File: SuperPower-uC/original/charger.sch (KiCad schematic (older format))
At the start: 34 parts, among them J1 Conn_01x02_Male, J2 Conn_01x02_Male, Q1 Q_NMOS_DGS, Q2 Q_NMOS_DGS, Q3 Q_NMOS_DGS, Q4 Q_PMOS_DGS, U1 LTC4162-L

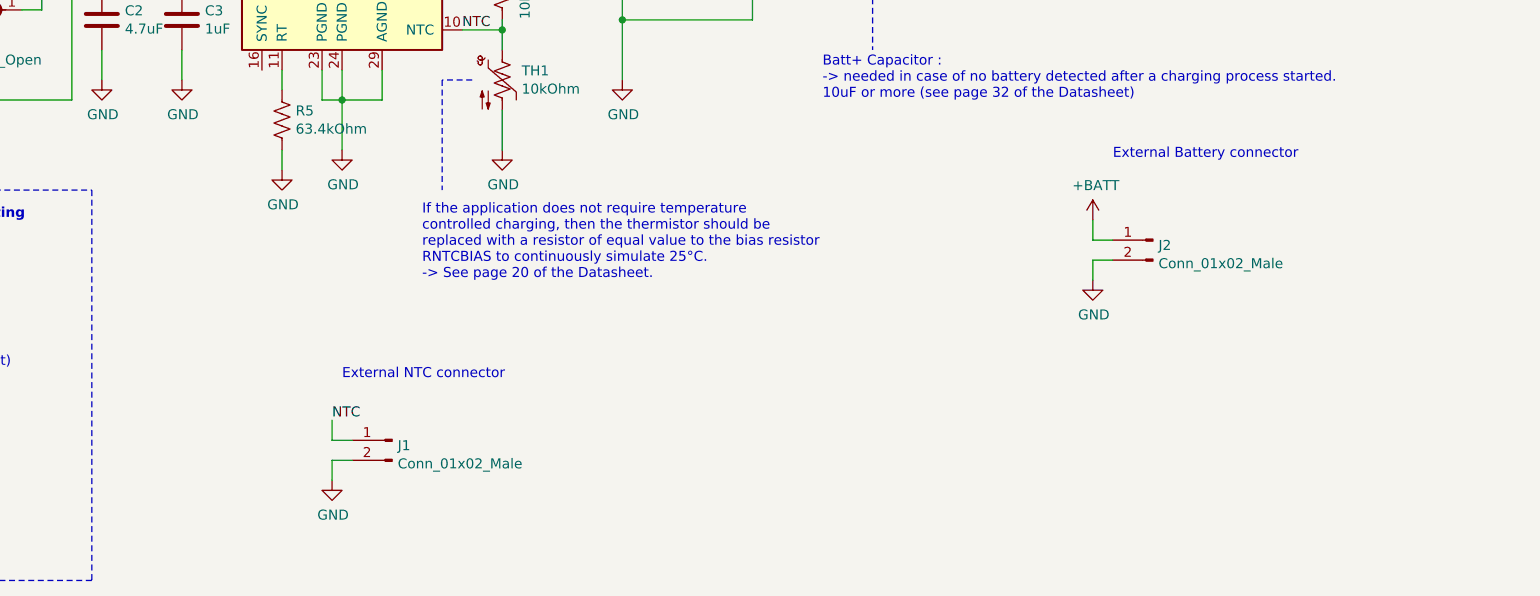
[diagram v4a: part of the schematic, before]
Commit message: Add default 1 cell settings
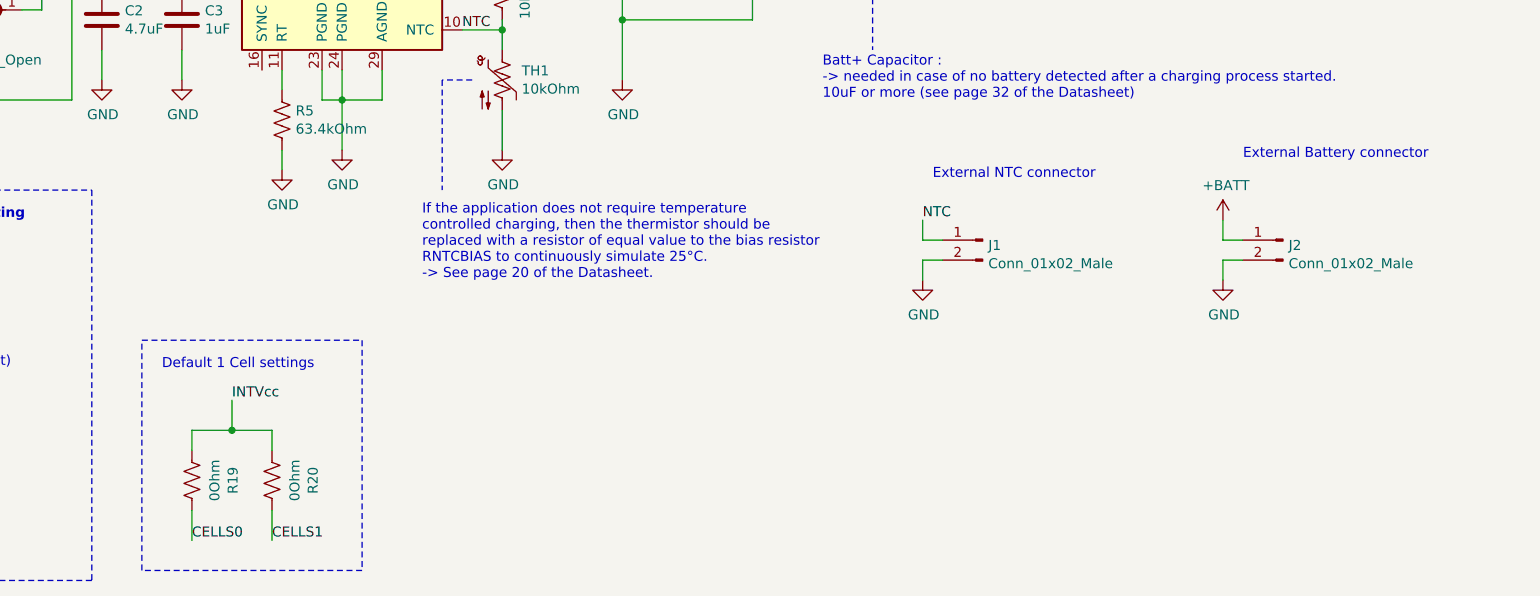
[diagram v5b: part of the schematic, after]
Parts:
- added R19, R20: 0Ohm, symbol Device:R_US
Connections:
- net CELLS0: now also R19.1
- net CELLS1: now also R20.1
- net INTVcc: now also R19.2, R20.2
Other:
- note added: "Default 1 Cell settings"
- moved on the sheet: J1, J2
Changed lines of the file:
@@
 L Connector:Conn_01x02_Male J1
 U 1 1 5F8314D1
-P 5850 6950
-F 0 "J1" H 5822 6924 50  0000 R CNN
-F 1 "Conn_01x02_Male" H 5822 6833 50  0000 R CNN
-F 2 "" H 5850 6950 50  0001 C CNN
-F 3 "~" H 5850 6950 50  0001 C CNN
-	1    5850 6950
+P 8800 5950
+F 0 "J1" H 8772 5924 50  0000 R CNN
+F 1 "Conn_01x02_Male" H 8772 5833 50  0000 R CNN
+F 2 "" H 8800 5950 50  0001 C CNN
+F 3 "~" H 8800 5950 50  0001 C CNN
+	1    8800 5950
 	-1   0    0    -1
 $EndComp
@@
 L power:GND #PWR07
 U 1 1 5F832657
-P 5550 7150
-F 0 "#PWR07" H 5550 6900 50  0001 C CNN
-F 1 "GND" H 5555 6977 50  0000 C CNN
-F 2 "" H 5550 7150 50  0001 C CNN
-F 3 "" H 5550 7150 50  0001 C CNN
-	1    5550 7150
-	1    0    0    -1
-$EndComp
-Wire Wire Line
-	5550 7150 5550 7050
-Wire Wire Line
-	5550 7050 5650 7050
-Wire Wire Line
-	5650 6950 5550 6950
-Wire Wire Line
-	5550 6950 5550 6850
-Text Label 5550 6850 0    50   ~ 0
+P 8500 6150
+F 0 "#PWR07" H 8500 5900 50  0001 C CNN
+F 1 "GND" H 8505 5977 50  0000 C CNN
+F 2 "" H 8500 6150 50  0001 C CNN
+F 3 "" H 8500 6150 50  0001 C CNN
+	1    8500 6150
+	1    0    0    -1
+$EndComp
+Wire Wire Line
+	8500 6150 8500 6050
+Wire Wire Line
+	8500 6050 8600 6050
+Wire Wire Line
+	8600 5950 8500 5950
+Wire Wire Line
+	8500 5950 8500 5850
+Text Label 8500 5850 0    50   ~ 0
 NTC
 Connection ~ 3150 2700
@@
 Wire Wire Line
 	2500 2700 3150 2700
-Text Notes 5600 6650 0    50   ~ 0
+Text Notes 8550 5650 0    50   ~ 0
 External NTC connector
 Wire Notes Line
@@
 L Connector:Conn_01x02_Male J2
 U 1 1 5F831EE9
-P 9650 5950
-F 0 "J2" H 9622 5924 50  0000 R CNN
-F 1 "Conn_01x02_Male" H 9622 5833 50  0000 R CNN
-F 2 "" H 9650 5950 50  0001 C CNN
-F 3 "~" H 9650 5950 50  0001 C CNN
-	1    9650 5950
+P 10300 5950
+F 0 "J2" H 10272 5924 50  0000 R CNN
+F 1 "Conn_01x02_Male" H 10272 5833 50  0000 R CNN
+F 2 "" H 10300 5950 50  0001 C CNN
+F 3 "~" H 10300 5950 50  0001 C CNN
+	1    10300 5950
 	-1   0    0    -1
 $EndComp
@@
 L power:GND #PWR016
 U 1 1 5F831EF3
-P 9350 6150
-F 0 "#PWR016" H 9350 5900 50  0001 C CNN
-F 1 "GND" H 9355 5977 50  0000 C CNN
-F 2 "" H 9350 6150 50  0001 C CNN
-F 3 "" H 9350 6150 50  0001 C CNN
-	1    9350 6150
-	1    0    0    -1
-$EndComp
-Wire Wire Line
-	9350 6150 9350 6050
-Wire Wire Line
-	9350 6050 9450 6050
-Wire Wire Line
-	9450 5950 9350 5950
-Wire Wire Line
-	9350 5950 9350 5850
+P 10000 6150
+F 0 "#PWR016" H 10000 5900 50  0001 C CNN
+F 1 "GND" H 10005 5977 50  0000 C CNN
+F 2 "" H 10000 6150 50  0001 C CNN
+F 3 "" H 10000 6150 50  0001 C CNN
+	1    10000 6150
+	1    0    0    -1
+$EndComp
+Wire Wire Line
+	10000 6150 10000 6050
+Wire Wire Line
+	10000 6050 10100 6050
+Wire Wire Line
+	10100 5950 10000 5950
+Wire Wire Line
+	10000 5950 10000 5850
 $Comp
 L power:+BATT #PWR015
 U 1 1 5F837E39
-P 9350 5850
-F 0 "#PWR015" H 9350 5700 50  0001 C CNN
-F 1 "+BATT" H 9365 6023 50  0000 C CNN
-F 2 "" H 9350 5850 50  0001 C CNN
-F 3 "" H 9350 5850 50  0001 C CNN
-	1    9350 5850
-	1    0    0    -1
-$EndComp
-Text Notes 9450 5550 0    50   ~ 0
+P 10000 5850
+F 0 "#PWR015" H 10000 5700 50  0001 C CNN
+F 1 "+BATT" H 10015 6023 50  0000 C CNN
+F 2 "" H 10000 5850 50  0001 C CNN
+F 3 "" H 10000 5850 50  0001 C CNN
+	1    10000 5850
+	1    0    0    -1
+$EndComp
+Text Notes 10100 5550 0    50   ~ 0
 External Battery connector
 $Comp
@@
 Text Notes 3200 3850 0    50   ~ 0
 TODO : Add Hierarchical Block Connector ->
+$Comp
+L Device:R_US R19
+U 1 1 5F845E81
+P 4850 7150
+F 0 "R19" V 4645 7150 50  0000 C CNN
+F 1 "0Ohm" V 4736 7150 50  0000 C CNN
+F 2 "" V 4890 7140 50  0001 C CNN
+F 3 "~" H 4850 7150 50  0001 C CNN
+	1    4850 7150
+	-1   0    0    1
+$EndComp
+$Comp
+L Device:R_US R20
+U 1 1 5F846819
+P 5250 7150
+F 0 "R20" V 5045 7150 50  0000 C CNN
+F 1 "0Ohm" V 5136 7150 50  0000 C CNN
+F 2 "" V 5290 7140 50  0001 C CNN
+F 3 "~" H 5250 7150 50  0001 C CNN
+	1    5250 7150
+	-1   0    0    1
+$EndComp
+Wire Wire Line
+	4850 7300 4850 7450
+Wire Wire Line
+	5250 7450 5250 7300
+Wire Wire Line
+	4850 7000 4850 6900
+Wire Wire Line
+	5250 7000 5250 6900
+Text Label 4850 7450 0    50   ~ 0
+CELLS0
+Text Label 5250 7450 0    50   ~ 0
+CELLS1
+Text Notes 4700 6600 0    50   ~ 0
+Default 1 Cell settings
+Wire Wire Line
+	4850 6900 5050 6900
+Wire Wire Line
+	5050 6750 5050 6900
+Connection ~ 5050 6900
+Wire Wire Line
+	5050 6900 5250 6900
+Text Label 5050 6750 0    50   ~ 0
+INTVcc
+Wire Notes Line
+	4600 6450 5700 6450
+Wire Notes Line
+	5700 6450 5700 7600
+Wire Notes Line
+	5700 7600 4600 7600
+Wire Notes Line
+	4600 7600 4600 6450
 $EndSCHEMATC

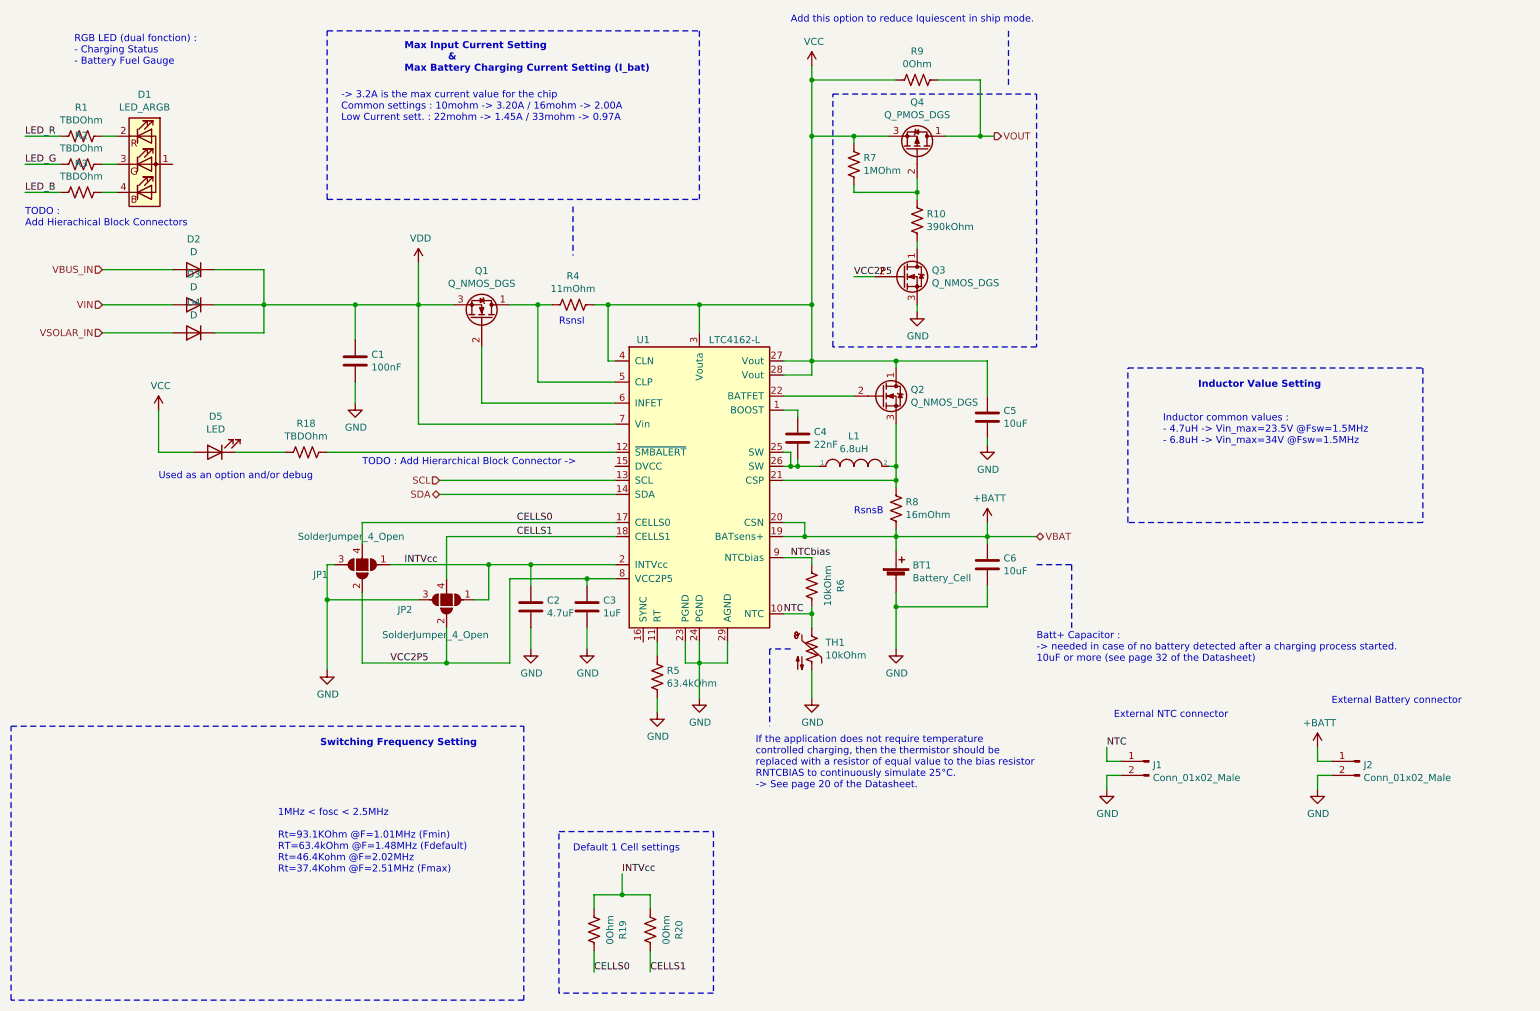
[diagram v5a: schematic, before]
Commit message: Update components annotations
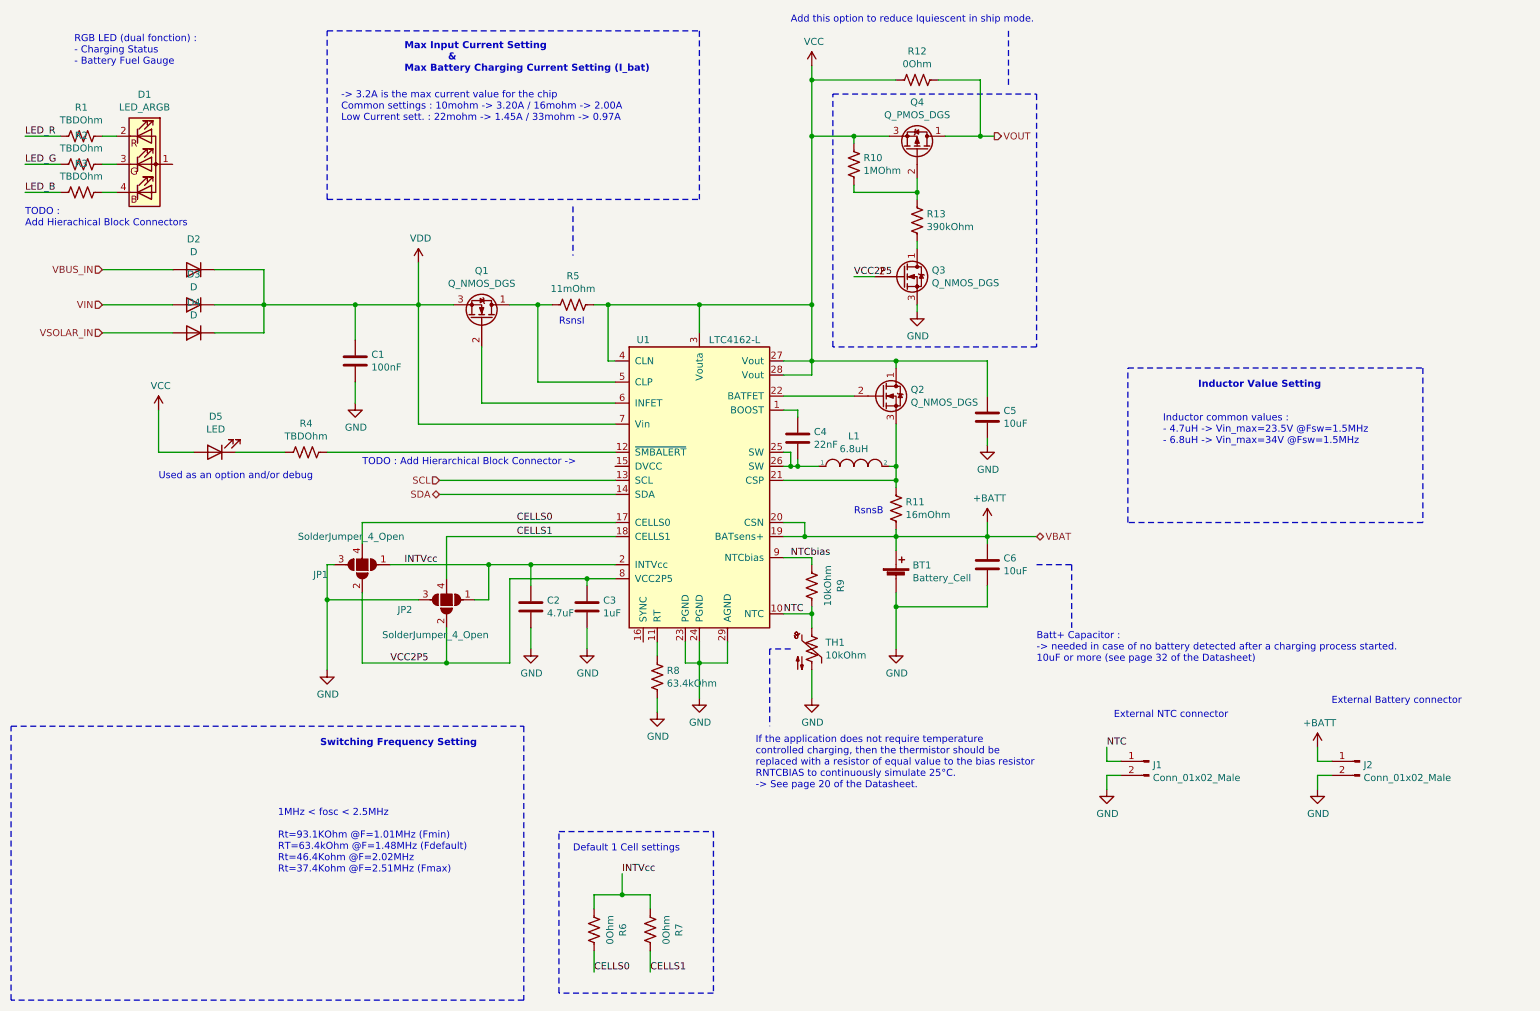
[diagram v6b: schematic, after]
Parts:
- renumbered R7 to R10, R8 to R11, R9 to R12, R10 to R13, R18 to R4, R4 to R5, R19 to R6, R20 to R7, R5 to R8, R6 to R9
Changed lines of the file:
@@
 $EndComp
 $Comp
-L Device:R_US R4
+L Device:R_US R5
 U 1 1 5F743F05
 P 4700 2700
-F 0 "R4" V 4495 2700 50  0000 C CNN
+F 0 "R5" V 4495 2700 50  0000 C CNN
 F 1 "11mOhm" V 4586 2700 50  0000 C CNN
 F 2 "" V 4740 2690 50  0001 C CNN
@@
 $EndComp
 $Comp
-L power:VDD #PWR03
+L power:VDD #PWR04
 U 1 1 5F7457C8
 P 3600 2400
-F 0 "#PWR03" H 3600 2250 50  0001 C CNN
+F 0 "#PWR04" H 3600 2250 50  0001 C CNN
 F 1 "VDD" H 3615 2573 50  0000 C CNN
 F 2 "" H 3600 2400 50  0001 C CNN
@@
 Connection ~ 4950 2700
 $Comp
-L power:GND #PWR02
+L power:GND #PWR03
 U 1 1 5F75199B
 P 3150 3400
-F 0 "#PWR02" H 3150 3150 50  0001 C CNN
+F 0 "#PWR03" H 3150 3150 50  0001 C CNN
 F 1 "GND" H 3155 3227 50  0000 C CNN
 F 2 "" H 3150 3400 50  0001 C CNN
@@
 	7000 4300 7000 4350
 $Comp
-L Device:R_US R8
+L Device:R_US R11
 U 1 1 5F7476B1
 P 7000 4150
-F 0 "R8" H 7068 4196 50  0000 L CNN
+F 0 "R11" H 7068 4196 50  0000 L CNN
 F 1 "16mOhm" H 7068 4105 50  0000 L CNN
 F 2 "" V 7040 4140 50  0001 C CNN
@@
 	7000 3950 7000 4000
 $Comp
-L Device:R_US R6
+L Device:R_US R9
 U 1 1 5F76C5B8
 P 6400 4700
-F 0 "R6" V 6195 4700 50  0000 C CNN
+F 0 "R9" V 6195 4700 50  0000 C CNN
 F 1 "10kOhm" V 6286 4700 50  0000 C CNN
 F 2 "" V 6440 4690 50  0001 C CNN
@@
 	6400 5000 6400 4900
 $Comp
-L power:GND #PWR06
+L power:GND #PWR07
 U 1 1 5F77962A
 P 5300 5600
-F 0 "#PWR06" H 5300 5350 50  0001 C CNN
+F 0 "#PWR07" H 5300 5350 50  0001 C CNN
 F 1 "GND" H 5305 5427 50  0000 C CNN
 F 2 "" H 5300 5600 50  0001 C CNN
@@
 $EndComp
 $Comp
-L Device:R_US R5
+L Device:R_US R8
 U 1 1 5F779EA2
 P 5300 5350
-F 0 "R5" H 5232 5304 50  0000 R CNN
+F 0 "R8" H 5232 5304 50  0000 R CNN
 F 1 "63.4kOhm" H 5232 5395 50  0000 R CNN
 F 2 "" V 5340 5340 50  0001 C CNN
@@
 $EndComp
 $Comp
-L power:GND #PWR04
+L power:GND #PWR05
 U 1 1 5F75A8F8
 P 4400 5150
-F 0 "#PWR04" H 4400 4900 50  0001 C CNN
+F 0 "#PWR05" H 4400 4900 50  0001 C CNN
 F 1 "GND" H 4405 4977 50  0000 C CNN
 F 2 "" H 4400 5150 50  0001 C CNN
@@
 $EndComp
 $Comp
-L power:GND #PWR05
+L power:GND #PWR06
 U 1 1 5F75ACE4
 P 4800 5150
-F 0 "#PWR05" H 4800 4900 50  0001 C CNN
+F 0 "#PWR06" H 4800 4900 50  0001 C CNN
 F 1 "GND" H 4805 4977 50  0000 C CNN
 F 2 "" H 4800 5150 50  0001 C CNN
@@
 	3200 5250 3800 5250
 $Comp
-L power:GND #PWR01
+L power:GND #PWR02
 U 1 1 5F75B0A7
 P 2950 5300
-F 0 "#PWR01" H 2950 5050 50  0001 C CNN
+F 0 "#PWR02" H 2950 5050 50  0001 C CNN
 F 1 "GND" H 2955 5127 50  0000 C CNN
 F 2 "" H 2950 5300 50  0001 C CNN
@@
 $EndComp
 $Comp
-L power:GND #PWR07
+L power:GND #PWR015
 U 1 1 5F832657
 P 8500 6150
-F 0 "#PWR07" H 8500 5900 50  0001 C CNN
+F 0 "#PWR015" H 8500 5900 50  0001 C CNN
 F 1 "GND" H 8505 5977 50  0000 C CNN
 F 2 "" H 8500 6150 50  0001 C CNN
@@
 $EndComp
 $Comp
-L Device:R_US R10
+L Device:R_US R13
 U 1 1 5F8508E1
 P 7150 2100
-F 0 "R10" H 7218 2146 50  0000 L CNN
+F 0 "R13" H 7218 2146 50  0000 L CNN
 F 1 "390kOhm" H 7218 2055 50  0000 L CNN
 F 2 "" V 7190 2090 50  0001 C CNN
@@
 	7150 2300 7150 2250
 $Comp
-L Device:R_US R7
+L Device:R_US R10
 U 1 1 5F85C6FA
 P 6700 1700
-F 0 "R7" H 6768 1746 50  0000 L CNN
+F 0 "R10" H 6768 1746 50  0000 L CNN
 F 1 "1MOhm" H 6768 1655 50  0000 L CNN
 F 2 "" V 6740 1690 50  0001 C CNN
@@
 $EndComp
 $Comp
-L power:GND #PWR016
+L power:GND #PWR017
 U 1 1 5F831EF3
 P 10000 6150
-F 0 "#PWR016" H 10000 5900 50  0001 C CNN
+F 0 "#PWR017" H 10000 5900 50  0001 C CNN
 F 1 "GND" H 10005 5977 50  0000 C CNN
 F 2 "" H 10000 6150 50  0001 C CNN
@@
 	10000 5950 10000 5850
 $Comp
-L power:+BATT #PWR015
+L power:+BATT #PWR016
 U 1 1 5F837E39
 P 10000 5850
-F 0 "#PWR015" H 10000 5700 50  0001 C CNN
+F 0 "#PWR016" H 10000 5700 50  0001 C CNN
 F 1 "+BATT" H 10015 6023 50  0000 C CNN
 F 2 "" H 10000 5850 50  0001 C CNN
@@
 External Battery connector
 $Comp
-L Device:R_US R9
+L Device:R_US R12
 U 1 1 5F8322FE
 P 7150 1100
-F 0 "R9" V 6945 1100 50  0000 C CNN
+F 0 "R12" V 6945 1100 50  0000 C CNN
 F 1 "0Ohm" V 7036 1100 50  0000 C CNN
 F 2 "" V 7190 1090 50  0001 C CNN
@@
 $EndComp
 $Comp
-L Device:R_US R18
+L Device:R_US R4
 U 1 1 5F84595F
 P 2800 3750
-F 0 "R18" V 2595 3750 50  0000 C CNN
+F 0 "R4" V 2595 3750 50  0000 C CNN
 F 1 "TBDOhm" V 2686 3750 50  0000 C CNN
 F 2 "" V 2840 3740 50  0001 C CNN
@@
 	2300 3750 2650 3750
 $Comp
-L power:VCC #PWR027
+L power:VCC #PWR01
 U 1 1 5F851525
 P 1750 3450
-F 0 "#PWR027" H 1750 3300 50  0001 C CNN
+F 0 "#PWR01" H 1750 3300 50  0001 C CNN
 F 1 "VCC" H 1765 3623 50  0000 C CNN
 F 2 "" H 1750 3450 50  0001 C CNN
@@
 TODO : Add Hierarchical Block Connector ->
 $Comp
-L Device:R_US R19
+L Device:R_US R6
 U 1 1 5F845E81
 P 4850 7150
-F 0 "R19" V 4645 7150 50  0000 C CNN
+F 0 "R6" V 4645 7150 50  0000 C CNN
 F 1 "0Ohm" V 4736 7150 50  0000 C CNN
 F 2 "" V 4890 7140 50  0001 C CNN
@@
 $EndComp
 $Comp
-L Device:R_US R20
+L Device:R_US R7
 U 1 1 5F846819
 P 5250 7150
-F 0 "R20" V 5045 7150 50  0000 C CNN
+F 0 "R7" V 5045 7150 50  0000 C CNN
 F 1 "0Ohm" V 5136 7150 50  0000 C CNN
 F 2 "" V 5290 7140 50  0001 C CNN

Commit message: Delete 3 tmp files...
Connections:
- net +BATT: no longer BT1.1 (+), C6.1, R11.2, U1.19 (BATsens+), U1.20 (CSN)
- new net VBAT: BT1.1 (+), C6.1, R11.2, U1.19 (BATsens+), U1.20 (CSN)
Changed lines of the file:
@@
-$EndComp
-$Comp
-L power:+BATT #PWR014
-U 1 1 5F744E2E
-P 7650 4250
-F 0 "#PWR014" H 7650 4100 50  0001 C CNN
-F 1 "+BATT" H 7665 4423 50  0000 C CNN
-F 2 "" H 7650 4250 50  0001 C CNN
-F 3 "" H 7650 4250 50  0001 C CNN
-	1    7650 4250
-	1    0    0    -1
 $EndComp
 $Comp
@@
 Wire Wire Line
 	7000 4850 7000 4750
-Wire Wire Line
-	7650 4250 7650 4350
 Connection ~ 7650 4350
 Wire Wire Line

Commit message: Add components renaming
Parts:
- renumbered BT1 to BT2, C1 to C2, C2 to C3, C3 to C4, C4 to C5, C5 to C6, C6 to C7, J1 to J2, J2 to J3, Q1 to Q2, Q2 to Q3, Q3 to Q4, Q4 to Q5, R8 to R10, R9 to R11, R10 to R12, R11 to R13, R12 to R14, R13 to R15, R1 to R3, R2 to R4, R3 to R5, R4 to R6, R5 to R7, R6 to R8, R7 to R9, U1 to U2
